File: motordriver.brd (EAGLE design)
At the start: 100 x 80 mm, 101 parts, among them J1 CONNECTOR_MOTORS, J10 HEADER_1X3, J11 HEADER_1X3, J2 CONNECTOR_MOTORS, J3 CONNECTOR_MOTORS, J4 CONNECTOR_MOTORS, J5 HEADER_1X3, J6 HEADER_1X3, J7 HEADER_1X3, J8 HEADER_1X3, J9 CONNECTOR_MOTORS, Q1 MOSFET, Q10 MOSFET, Q11 MOSFET, Q12 MOSFET, Q13 MOSFET, Q14 MOSFET, Q15 MOSFET, Q16 MOSFET, Q2 MOSFET, Q3 MOSFET, Q4 MOSFET, Q5 MOSFET, Q6 MOSFET, Q7 MOSFET, Q8 MOSFET, Q9 MOSFET, U1 74XX139_PDIP, U10 IR2111_PDIP, U11 IR2111_PDIP, U12 7812_TO220, U2 TL084_PDIP, U3 7812_TO220, U4 IR2111_PDIP, U5 IR2111_PDIP, U6 IR2111_PDIP, U7 IR2111_PDIP, U8 IR2111_PDIP, U9 IR2111_PDIP

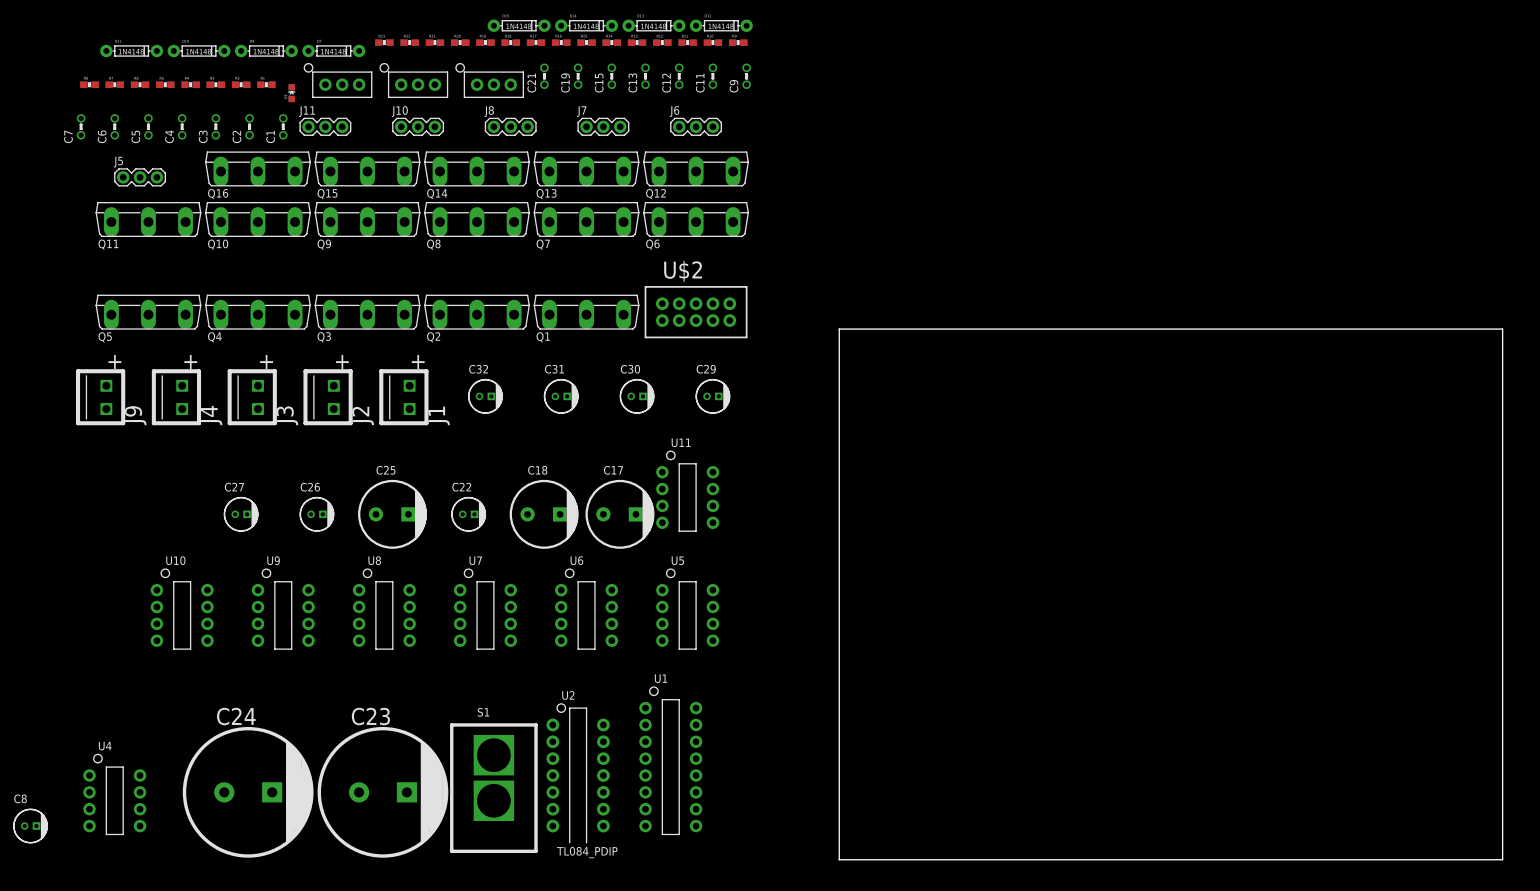
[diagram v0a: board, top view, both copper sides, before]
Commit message: Added PCB
Motor driver movie film for theaters part II
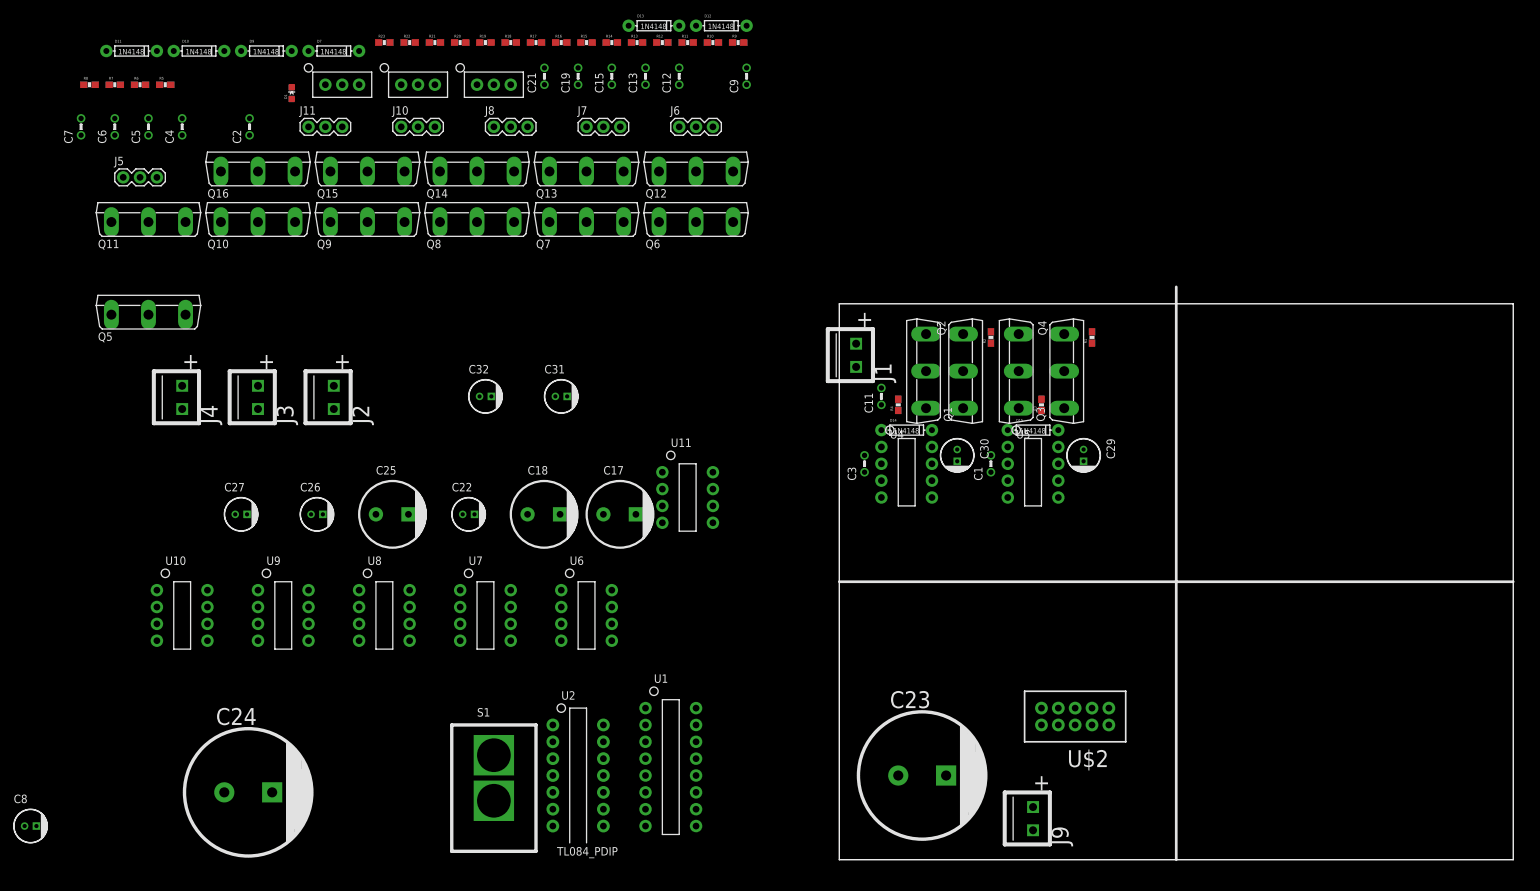
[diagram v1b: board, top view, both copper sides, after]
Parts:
- moved J9 153.5 mm to (29.2, 6.35)
- moved R3 133.5 mm to (30.5, 68.6), turned to 90 degrees
- moved R1 130.2 mm to (38.1, 78.7), turned to 90 degrees
- moved U4 129.2 mm to (6.35, 62.2)
- moved Q4 120.9 mm to (33.0, 73.7), turned to 270 degrees
- moved R2 119.3 mm to (22.9, 78.7), turned to 90 degrees
- moved C1 118.2 mm to (22.9, 58.4)
- moved R4 117.1 mm to (8.89, 68.6), turned to 90 degrees
- moved C3 110.2 mm to (3.81, 58.4)
- moved Q3 99.4 mm to (27.9, 73.7), turned to 90 degrees
- moved D15 98.6 mm to (29.2, 64.8)
- moved U$2 83.6 mm to (35.6, 21.6), turned to 180 degrees
- moved C23 81.3 mm to (8.89, 12.7)
- moved D14 77.8 mm to (10.2, 64.8)
- moved Q2 72.8 mm to (17.8, 73.7), turned to 270 degrees
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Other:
- board size 100 x 80 mm -> 101.6 x 83.8 mm

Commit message: Arranged H-bridge components
Looks like there will be enough space to fit the essential admin
components
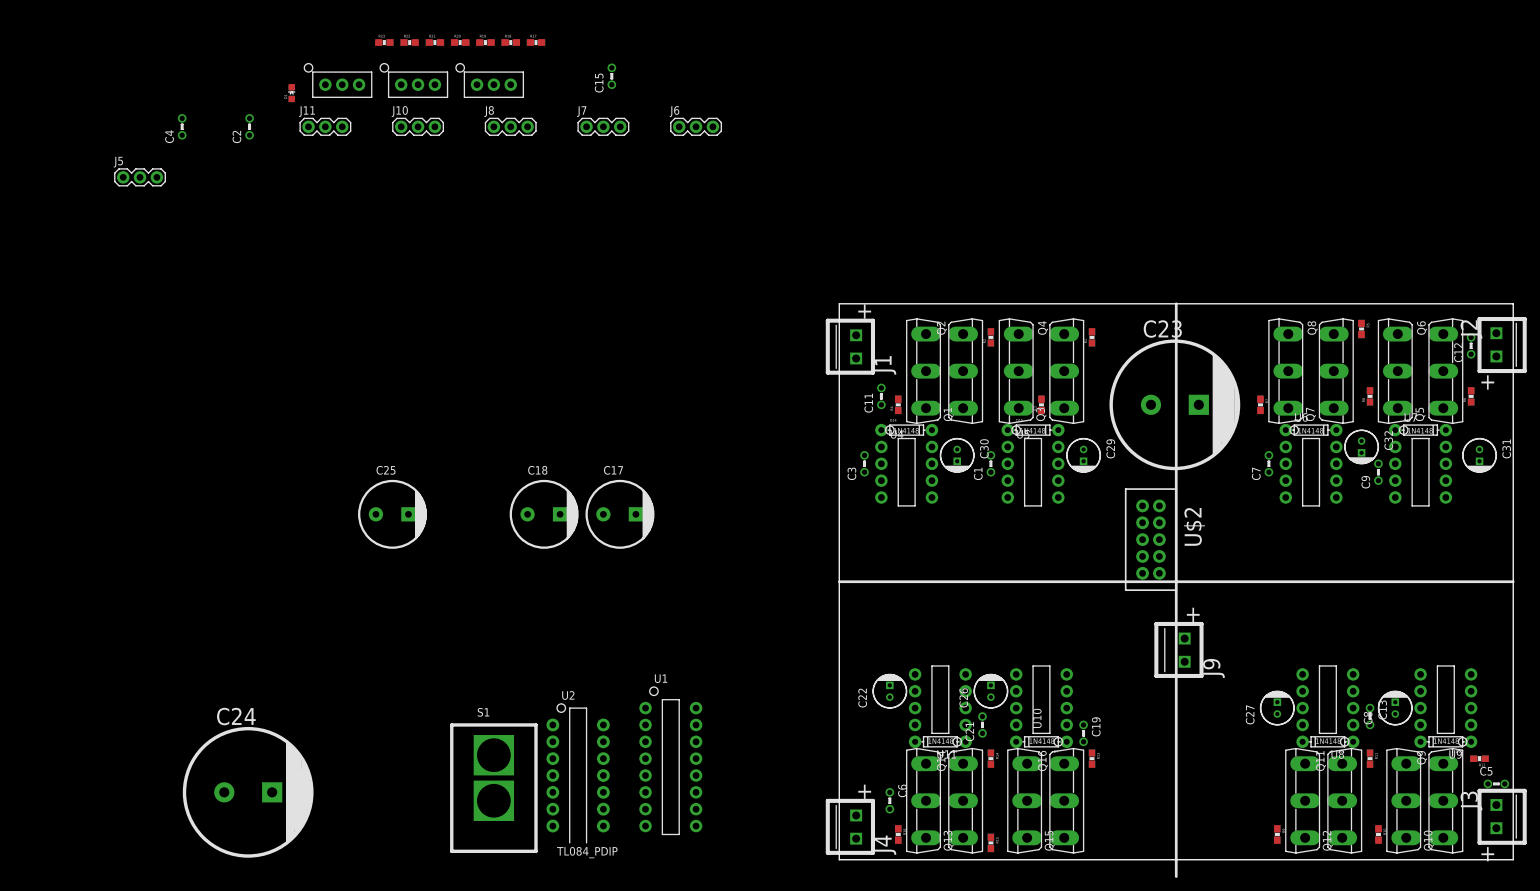
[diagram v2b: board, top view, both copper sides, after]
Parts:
- moved C5 224.4 mm to (97.8, 11.4), turned to 270 degrees
- moved D10 214.9 mm to (91.4, 17.8), turned to 180 degrees
- moved D11 208.2 mm to (73.7, 17.8), turned to 180 degrees
- moved C8 206.5 mm to (83.8, 22.9), turned to 90 degrees
- moved R6 206.1 mm to (95.2, 69.8), turned to 90 degrees
- moved Q11 198.8 mm to (74.9, 8.89), turned to 270 degrees
- moved R8 198.7 mm to (80.0, 69.8), turned to 90 degrees
- moved J3 197.2 mm to (99.1, 6.35), turned to 180 degrees
- moved Q10 194.2 mm to (86.4, 8.89), turned to 90 degrees
- moved Q5 189.4 mm to (85.1, 73.7), turned to 90 degrees
- moved C7 186.1 mm to (64.8, 58.4)
- moved R5 184.1 mm to (78.7, 80.0), turned to 270 degrees
- moved U9 184.0 mm to (95.2, 20.3), turned to 180 degrees
- moved Q9 183.0 mm to (90.2, 8.89), turned to 270 degrees
- moved R7 179.3 mm to (63.5, 68.6), turned to 270 degrees
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
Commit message: Cap23 just got murde
I put it in the dirt or somethin
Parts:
- removed C23: CAP_2200U_63V, motordriverslib:RADIAL_18
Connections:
- net GND: no longer C23.-
- net VCC_12V: no longer C23.+
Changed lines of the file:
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@@
 <element name="C21" library="motordriverslib" package="2DIP" value="CAP_1U" x="21.59" y="19.05"/>
 <element name="C22" library="motordriverslib" package="RADIAL_5" value="CAP_330N_50V" x="7.62" y="25.4" rot="R90"/>
-<element name="C23" library="motordriverslib" package="RADIAL_18" value="CAP_2200U_63V" x="46.99" y="68.58"/>
 <element name="C24" library="motordriverslib" package="RADIAL_18" value="CAP_2200U_63V" x="-92.71" y="10.16"/>
 <element name="C25" library="motordriverslib" package="RADIAL_1O" value="CAP_330U_25V" x="-69.85" y="52.07"/>
@@
 <contactref element="C1" pad="P$2"/>
 <contactref element="D15" pad="A"/>
-<contactref element="C23" pad="+"/>
 <contactref element="C24" pad="+"/>
 <contactref element="U4" pad="VCC"/>
@@
 <wire x1="67.31" y1="64.77" x2="67.31" y2="62.23" width="0" layer="19" extent="1-1"/>
 <wire x1="64.77" y1="60.96" x2="67.31" y2="62.23" width="0" layer="19" extent="1-1"/>
-<wire x1="46.99" y1="68.58" x2="64.77" y2="60.96" width="0" layer="19" extent="1-1"/>
-<wire x1="25.4" y1="64.77" x2="46.99" y2="68.58" width="0" layer="19" extent="1-1"/>
-<wire x1="25.4" y1="62.23" x2="25.4" y2="64.77" width="0" layer="19" extent="1-1"/>
-<wire x1="22.86" y1="60.96" x2="25.4" y2="62.23" width="0" layer="19" extent="1-1"/>
-<wire x1="6.35" y1="62.23" x2="22.86" y2="60.96" width="0" layer="19" extent="1-1"/>
-<wire x1="6.35" y1="64.77" x2="6.35" y2="62.23" width="0" layer="19" extent="1-1"/>
-<wire x1="3.81" y1="60.96" x2="6.35" y2="62.23" width="0" layer="19" extent="1-1"/>
 <wire x1="80.01" y1="20.32" x2="81.28" y2="59.69" width="0" layer="19" extent="1-1"/>
 <wire x1="77.47" y1="20.32" x2="80.01" y2="20.32" width="0" layer="19" extent="1-1"/>
@@
 <wire x1="95.25" y1="20.32" x2="80.01" y2="20.32" width="0" layer="19" extent="1-1"/>
 <wire x1="95.25" y1="17.78" x2="95.25" y2="20.32" width="0" layer="19" extent="1-1"/>
+<wire x1="25.4" y1="62.23" x2="64.77" y2="60.96" width="0" layer="19" extent="1-1"/>
+<wire x1="25.4" y1="64.77" x2="25.4" y2="62.23" width="0" layer="19" extent="1-1"/>
+<wire x1="22.86" y1="60.96" x2="25.4" y2="62.23" width="0" layer="19" extent="1-1"/>
+<wire x1="6.35" y1="62.23" x2="22.86" y2="60.96" width="0" layer="19" extent="1-1"/>
+<wire x1="6.35" y1="64.77" x2="6.35" y2="62.23" width="0" layer="19" extent="1-1"/>
+<wire x1="3.81" y1="60.96" x2="6.35" y2="62.23" width="0" layer="19" extent="1-1"/>
 <wire x1="21.59" y1="21.59" x2="22.86" y2="60.96" width="0" layer="19" extent="1-1"/>
 <wire x1="19.05" y1="20.32" x2="21.59" y2="21.59" width="0" layer="19" extent="1-1"/>
@@
 <contactref element="C21" pad="P$1"/>
 <contactref element="U11" pad="COM"/>
-<contactref element="C23" pad="-"/>
 <contactref element="C24" pad="-"/>
 <contactref element="U$1" pad="GND"/>
@@
 <contactref element="J11" pad="1"/>
 <wire x1="67.691" y1="79.248" x2="84.201" y2="79.248" width="0" layer="19" extent="1-1"/>
-<wire x1="54.205" y1="68.58" x2="67.691" y2="79.248" width="0" layer="19" extent="1-1"/>
-<wire x1="64.77" y1="58.42" x2="54.205" y2="68.58" width="0" layer="19" extent="1-1"/>
+<wire x1="64.77" y1="58.42" x2="67.691" y2="79.248" width="0" layer="19" extent="1-1"/>
 <wire x1="67.31" y1="57.15" x2="64.77" y2="58.42" width="0" layer="19" extent="1-1"/>
 <wire x1="81.28" y1="57.15" x2="67.31" y2="57.15" width="0" layer="19" extent="1-1"/>
